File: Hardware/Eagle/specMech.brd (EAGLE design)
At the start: 142.2 x 121.9 mm, 82 parts, among them J1 PINHD-1X8-MOLEX-SHROUD, J2 Molex 0022232081, J3 PINHD-1X8-MOLEX-SHROUD, J4 PINHD-1X8-MOLEX-SHROUD, J5 XPORT, J6 Molex 0022232081, J7 Molex 0022232081, J8 Molex 0022232081, U1 MCP23008-E/SO, U10 ADS1115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

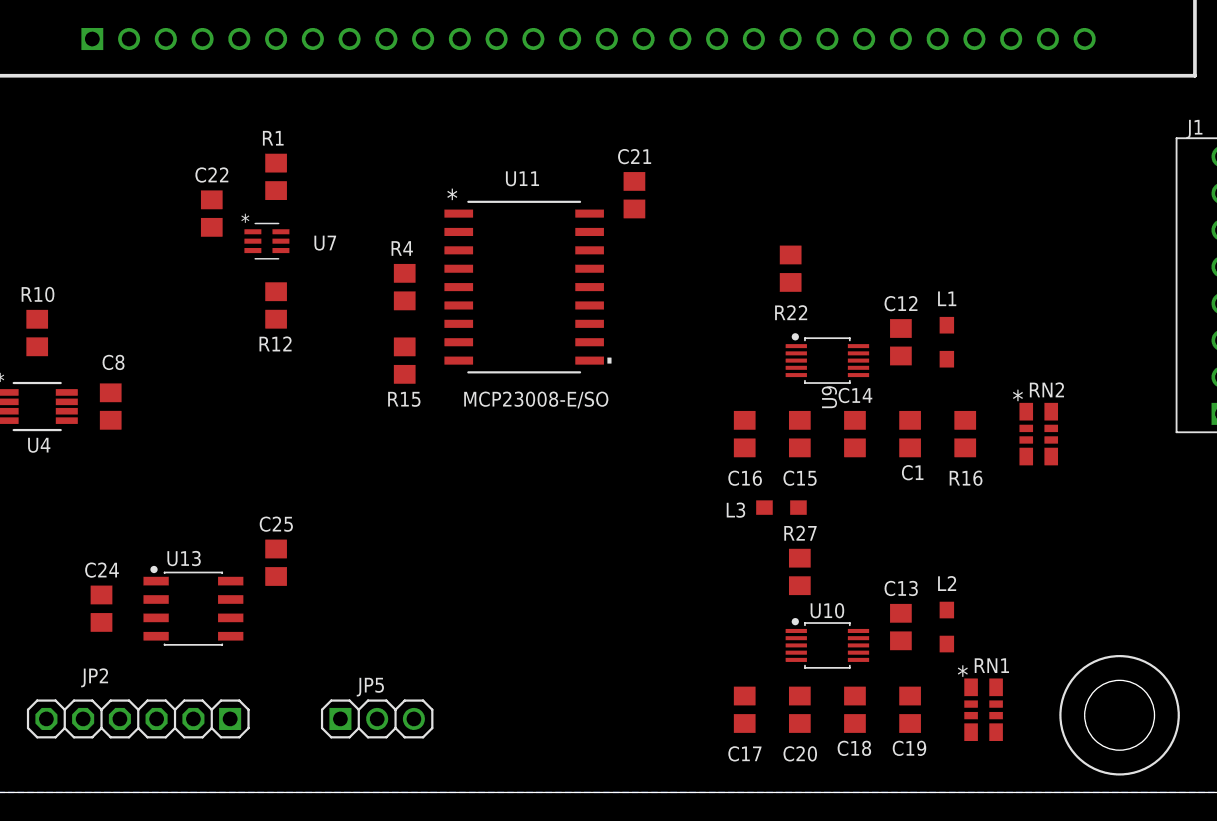
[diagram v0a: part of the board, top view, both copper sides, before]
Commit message: Rearrange ADC chips after brd file recovery
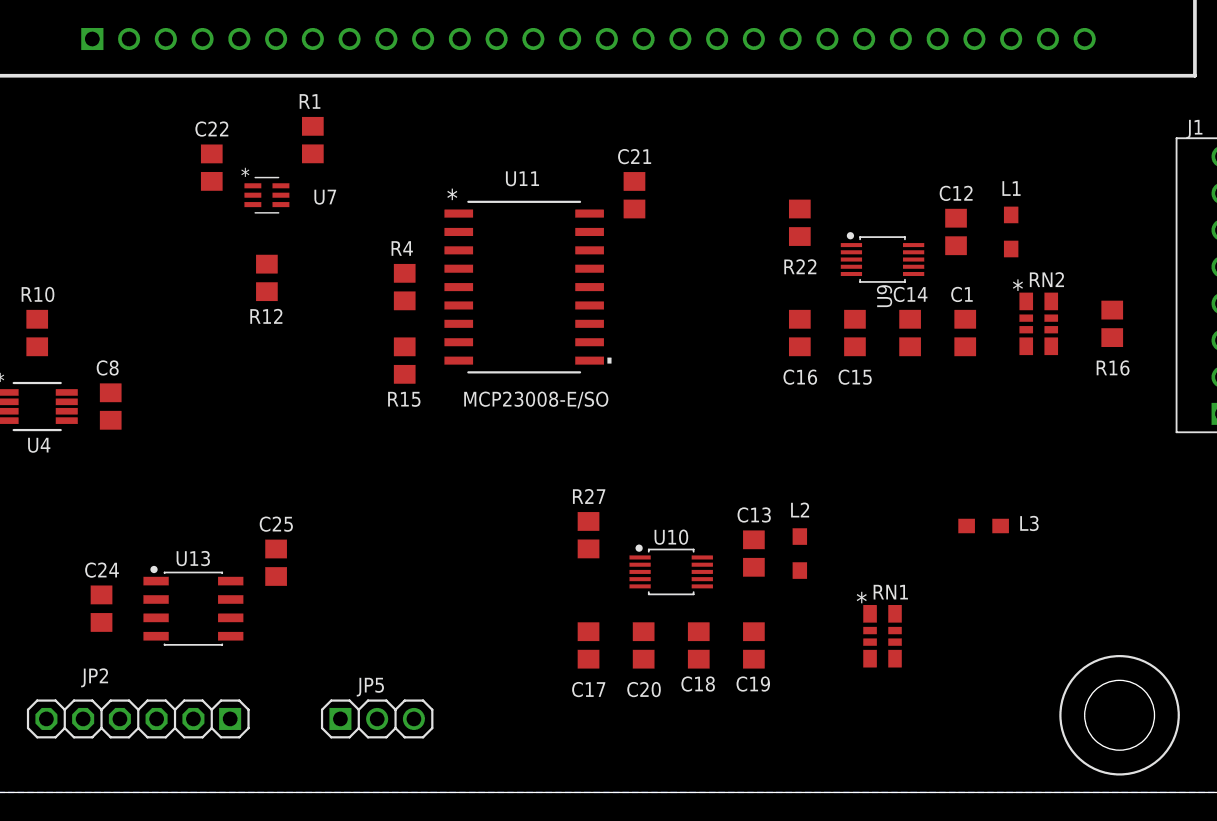
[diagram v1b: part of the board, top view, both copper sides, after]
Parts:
- moved R27 14.8 mm to (85.7, 17.8)
- moved L3 14.0 mm to (113.0, 18.4), turned to 0 degrees
- moved R16 12.7 mm to (121.9, 32.4)
- moved U10 11.9 mm to (91.4, 15.2)
- moved C17 11.7 mm to (85.7, 10.2)
- moved C18 11.7 mm to (93.3, 10.2)
- moved C19 11.7 mm to (97.2, 10.2)
- moved C20 11.7 mm to (89.5, 10.2)
- moved C13 11.4 mm to (97.2, 16.5)
- moved L2 11.4 mm to (100.3, 16.5)
- moved L1 8.82 mm to (114.9, 38.7)
- moved RN1 8.64 mm to (106.0, 10.8)
- moved C12 8.52 mm to (111.1, 38.7)
- moved C1 7.96 mm to (111.8, 31.8), turned to 90 degrees
- moved C14 7.96 mm to (108.0, 31.8)
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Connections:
- removed net 3.3V: C7.1, VR2.VOUT
- net +3.3V: now also C7.1, VR2.VOUT

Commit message: Rearranging parts
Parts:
- removed J2, J7: Molex 0022232081, AUmlib:1X08-MOLEX-SHROUD
- moved C23 19.9 mm to (130.2, 76.2)
- moved U12 19.9 mm to (125.7, 74.9)
- moved C25 3.24 mm to (64.8, 12.7), turned to 270 degrees
- moved C22 1.27 mm to (59.7, 41.9), turned to 270 degrees
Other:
- board text added: "AD590 on/off"
- board text added: "Beeper"
- board text added: "Collimator Motors"
- board text added: "LN2 Controller"
- board text added: "OLED Display"
- board text added: "Pneu Sensors"
- board text added: "Temperature"

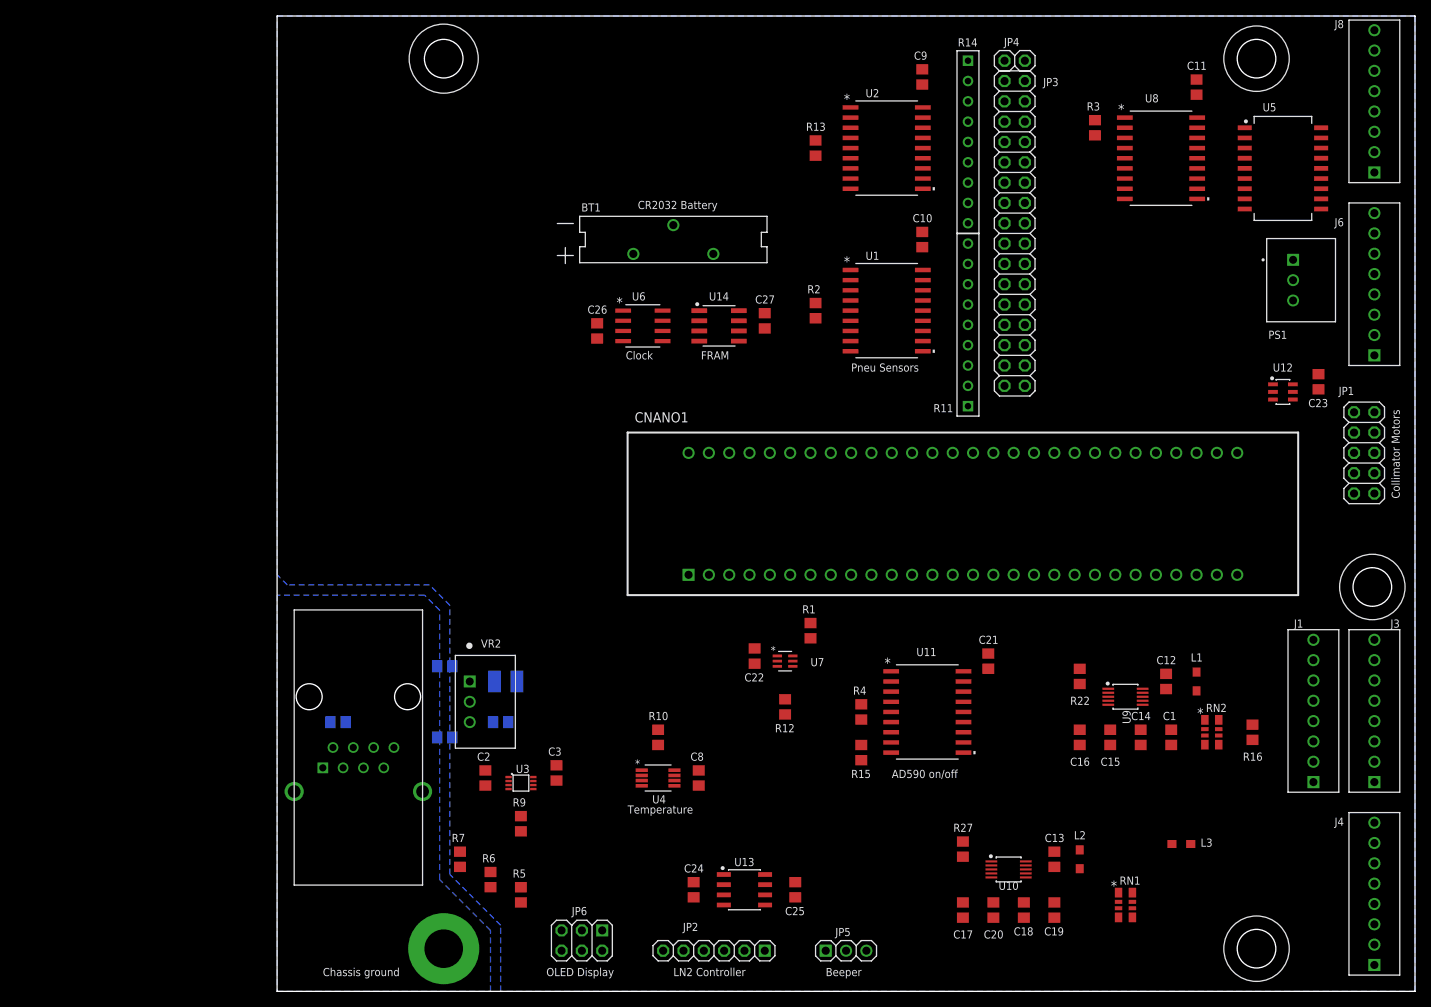
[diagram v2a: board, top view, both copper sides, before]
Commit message: Added ADC ground plane
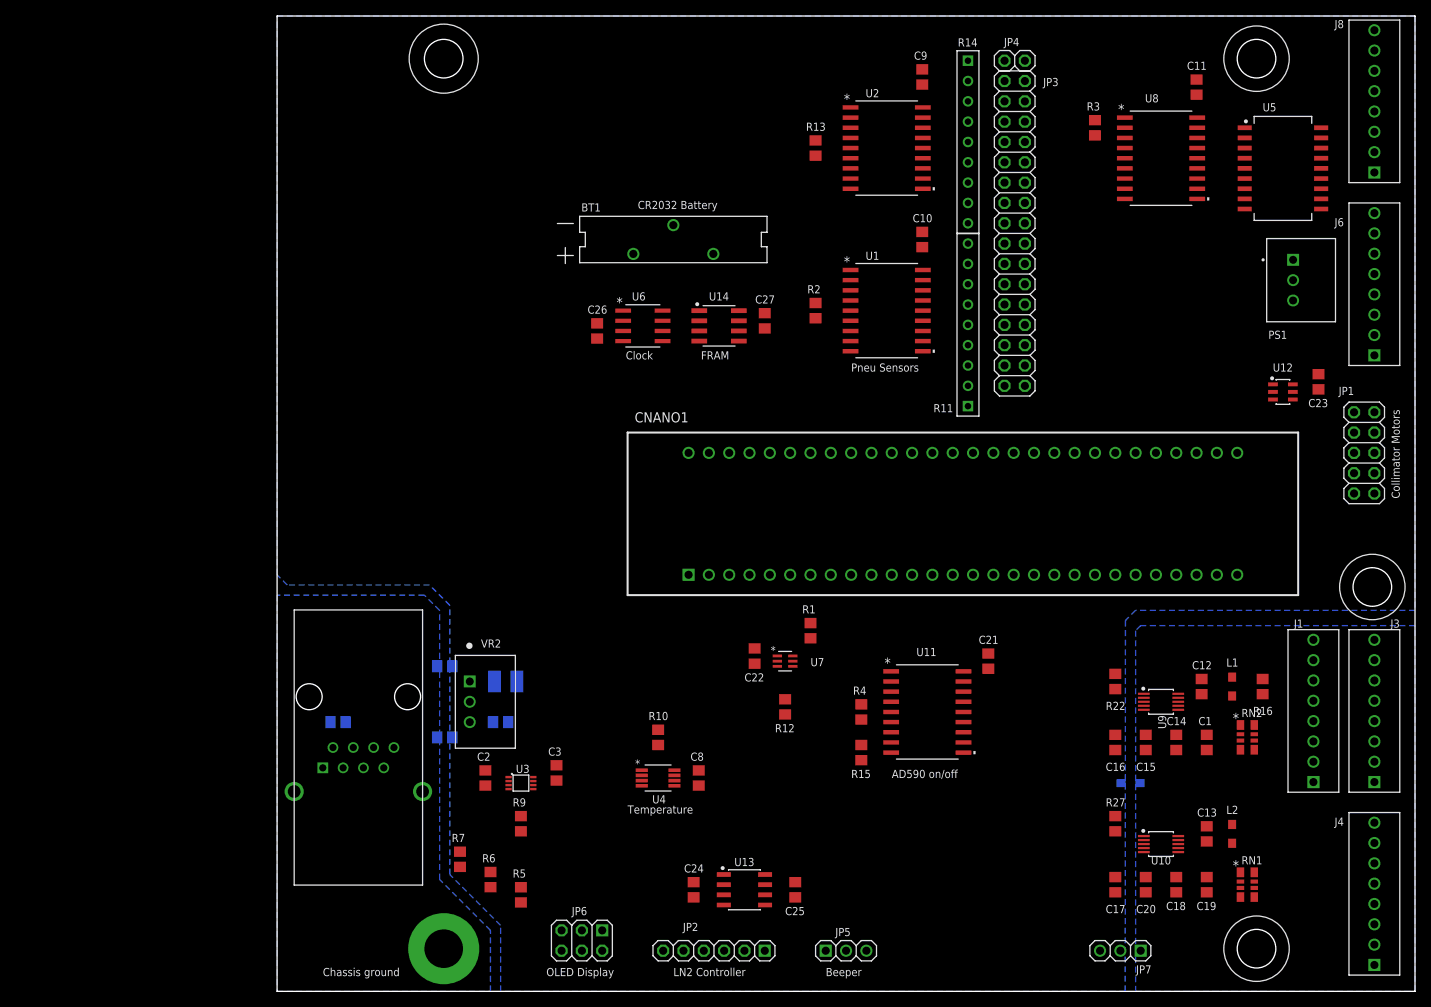
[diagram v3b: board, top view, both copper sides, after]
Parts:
- added JP7: (no value), AUmlib:1X03
- moved C17 19.3 mm to (104.8, 13.3)
- moved R27 19.3 mm to (104.8, 21.0)
- moved C18 19.3 mm to (112.4, 13.3)
- moved C19 19.3 mm to (116.2, 13.3)
- moved C20 19.3 mm to (108.6, 13.3)
- moved C13 19.3 mm to (116.2, 19.7)
- moved L2 19.3 mm to (119.4, 19.7)
- moved U10 19.3 mm to (110.5, 18.4)
- moved RN1 15.5 mm to (121.3, 13.3)
- moved L3 9.92 mm to (106.7, 26.0), flipped to the bottom, turned to 180 degrees
- moved R16 5.85 mm to (123.2, 38.1)
- moved C16 4.49 mm to (104.8, 31.1)
- moved R22 4.49 mm to (104.8, 38.7)
- moved C1 4.49 mm to (116.2, 31.1)
- moved C12 4.49 mm to (115.6, 38.1)
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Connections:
- net GND: now also JP7.2; no longer J1.P$1, J1.P$3, J1.P$5, J1.P$7, J4.P$1, J4.P$3, J4.P$5, J4.P$7
- net GND-ISO: now also J1.P$1, J1.P$3, J1.P$5, J1.P$7, J4.P$1, J4.P$3, J4.P$5, J4.P$7, JP7.1
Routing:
- added copper zone on layer 16, net GND-ISO

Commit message: Routed high current lines
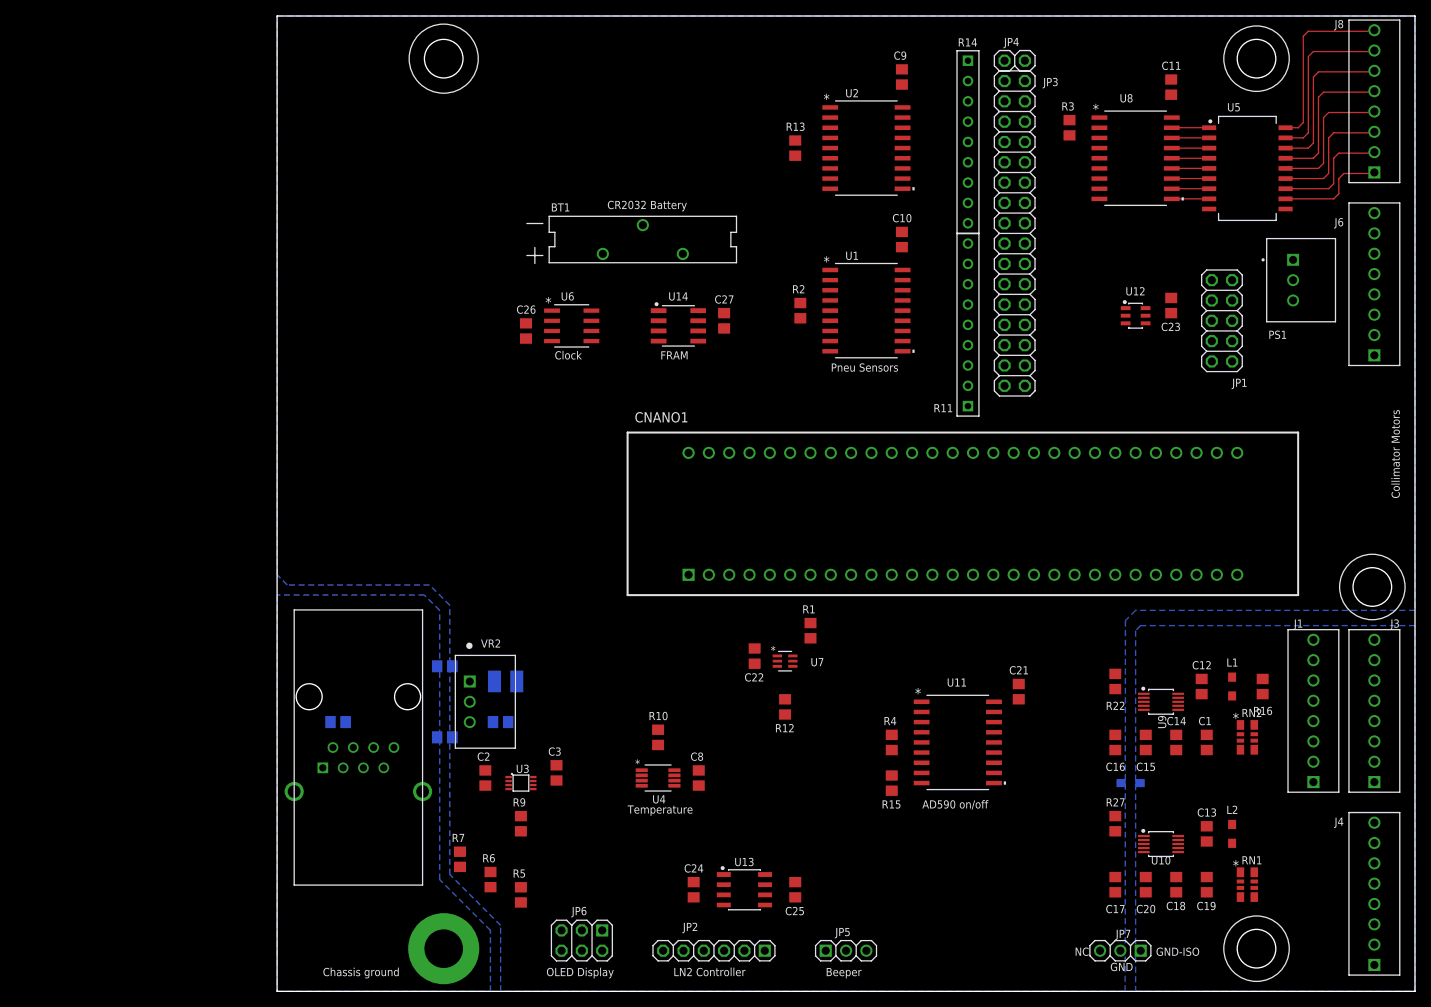
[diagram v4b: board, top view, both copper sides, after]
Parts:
- moved JP1 24.3 mm to (118.1, 83.8), turned to 270 degrees
- moved C23 20.7 mm to (111.8, 85.7)
- moved U12 20.7 mm to (107.3, 84.5)
- moved C26 8.89 mm to (31.1, 82.5)
- moved U6 8.89 mm to (36.8, 83.2)
- moved U11 5.39 mm to (85.1, 31.1)
- moved R15 5.39 mm to (76.8, 26.0)
- moved R4 5.39 mm to (76.8, 31.1)
- moved C21 5.39 mm to (92.7, 37.5)
- moved C27 5.08 mm to (55.9, 83.8)
- moved U14 5.08 mm to (50.2, 83.2)
- moved U5 4.45 mm to (121.3, 102.9)
- moved BT1 3.81 mm to (45.7, 94.0)
- moved C11 3.17 mm to (111.8, 113.0)
- moved R3 3.17 mm to (99.1, 108.0)
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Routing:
- net N$50: track 0.00 -> 22.5 mm
- net N$57: track 0.00 -> 21.2 mm
- net N$56: track 0.00 -> 19.9 mm
- net N$55: track 0.00 -> 18.7 mm
- net N$54: track 0.00 -> 17.4 mm
- net N$53: track 0.00 -> 16.1 mm
- net N$52: track 0.00 -> 14.9 mm
- net N$51: track 0.00 -> 13.6 mm
- net N$48: track 0.00 -> 4.68 mm
- net N$47: track 0.00 -> 4.68 mm
- net N$46: track 0.00 -> 4.68 mm
- net N$45: track 0.00 -> 4.68 mm
- net N$44: track 0.00 -> 4.68 mm
- net N$39: track 0.00 -> 4.68 mm
- net N$38: track 0.00 -> 4.68 mm
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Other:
- board text added: "GND"
- board text added: "GND-ISO"
- board text added: "NC"

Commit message: Wiring
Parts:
- moved C12 2.54 mm to (115.6, 40.6)
- moved L1 2.54 mm to (119.4, 40.6)
- moved R16 2.54 mm to (123.2, 40.6)
- moved R22 2.54 mm to (104.8, 41.3)
- moved U9 2.54 mm to (110.5, 38.7)
- moved C10 1.27 mm to (76.8, 94.0)
- moved C9 1.27 mm to (76.8, 114.3)
- moved R13 1.27 mm to (63.5, 105.4)
- moved R2 1.27 mm to (64.1, 85.1)
- moved U1 1.27 mm to (72.4, 85.1)
- moved U2 1.27 mm to (72.4, 105.4)
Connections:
- net N$19: now also JP1.3; no longer JP1.7
- net N$8: now also JP1.7; no longer JP1.3
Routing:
- net +5V: track 0.00 -> 94.1 mm
- net RC-RX: track 0.00 -> 48.6 mm
- net RC-TX: track 0.00 -> 47.2 mm
- net GND: track 0.00 -> 43.6 mm, vias 0 -> 17
- net +12V: track 0.00 -> 30.4 mm
- net N$16: track 0.00 -> 15.9 mm
- net N$1: track 0.00 -> 15.9 mm
- net N$9: track 0.00 -> 15.9 mm
- net N$22: track 0.00 -> 15.9 mm
- net N$10: track 0.00 -> 15.5 mm
- net N$21: track 0.00 -> 15.4 mm
- net N$2: track 0.00 -> 15.4 mm
- net N$15: track 0.00 -> 15.4 mm
- net N$20: track 0.00 -> 15.0 mm
- net N$11: track 0.00 -> 14.9 mm
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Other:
- board text added: "Collimator Motors USART"
- board text removed: "Collimator Motors"

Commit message: Wiring
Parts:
- moved R12 6.48 mm to (69.8, 36.8)
- moved C22 5.08 mm to (64.8, 41.9)
- moved U7 5.08 mm to (68.6, 41.3)
- moved R1 3.24 mm to (69.8, 45.7)
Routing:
- net SCL: track 0.00 -> 18.8 mm
- net GND: track 43.6 -> 58.6 mm, vias 17 -> 19
- net SDA: track 0.00 -> 11.6 mm
- net +5V: track 94.1 -> 97.2 mm

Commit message: Wiring
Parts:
- moved C18 3.86 mm to (116.2, 12.7)
- moved C19 3.86 mm to (112.4, 12.7)
- moved RN1 0.90 mm to (120.7, 12.7)
- moved C17 0.64 mm to (104.8, 12.7)
- moved C20 0.64 mm to (108.6, 12.7)
- moved L3 0.64 mm to (106.7, 25.4)
- moved C13 0.63 mm to (116.2, 19.1)
- moved L2 0.63 mm to (119.4, 19.1)
- moved R27 0.63 mm to (104.8, 20.3)
- turned C1 to 270 degrees
- turned C14 to 270 degrees
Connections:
- net GND: no longer C12.2, C13.2, U9.1
- net GND-ISO: now also C12.2, C13.2, U9.1
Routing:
- net N$69: track 0.00 -> 32.2 mm
- net A0B: track 0.00 -> 22.4 mm
- net N$68: track 0.00 -> 21.5 mm
- net GND-ISO: track 0.00 -> 19.9 mm, vias 0 -> 5
- net A1B: track 0.00 -> 18.0 mm
- net A3B: track 0.00 -> 17.8 mm
- net A2B: track 0.00 -> 16.2 mm
- net N$65: track 0.00 -> 15.8 mm
- net VBAT1: track 0.00 -> 10.0 mm
- net N$67: track 0.00 -> 9.05 mm
- net N$6: track 0.00 -> 6.96 mm
- net N$70: track 0.00 -> 4.08 mm

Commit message: Wiring
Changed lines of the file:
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@@
 </layers>
 <board>
-<fusionsync huburn="a.cGVyc29uYWw6dWUyZDgyNjcx" projecturn="a.cGVyc29uYWw6dWUyZDgyNjcxIzIwMTgxMjIwMTY2NDc1MjMx" f3durn="urn:adsk.wipprod:dm.lineage:_sV9k5X2SmWQ17yhuORBVg" pcbguid="" lastpulledtime="" lastsyncedchangeguid="" latestrevisionid="a685aebe-6f30-4309-919d-8c6f5bc8299c" lastsyncedrevisionid="a685aebe-6f30-4309-919d-8c6f5bc8299c" lastboardhashguid="185580c9-e881-60b1-63ba-49ad7843264c" lastpushedtime="2020-11-01T21:32:16Z" linktopcb3d="true"/>
+<fusionsync huburn="a.cGVyc29uYWw6dWUyZDgyNjcx" projecturn="a.cGVyc29uYWw6dWUyZDgyNjcxIzIwMTgxMjIwMTY2NDc1MjMx" f3durn="urn:adsk.wipprod:dm.lineage:_sV9k5X2SmWQ17yhuORBVg" pcbguid="" lastpulledtime="" lastsyncedchangeguid="" latestrevisionid="f88995e2-ef19-4b81-bcde-88b136ebe312" lastsyncedrevisionid="f88995e2-ef19-4b81-bcde-88b136ebe312" lastboardhashguid="351dc84e-53f2-6048-b294-c2d578f670e1" lastpushedtime="2020-11-02T02:08:29Z" linktopcb3d="true"/>
 <plain>
 <wire x1="0" y1="0" x2="142.24" y2="0" width="0" layer="20"/>
@@
 <contactref element="R11" pad="7"/>
 <wire x1="86.36" y1="88.392" x2="86.233" y2="88.265" width="0.1524" layer="1"/>
-<wire x1="83.82" y1="88.265" x2="81.915" y2="86.36" width="0.1524" layer="1"/>
-<wire x1="81.915" y1="86.36" x2="76.9112" y2="86.36" width="0.1524" layer="1"/>
-<wire x1="86.233" y1="88.265" x2="83.82" y2="88.265" width="0.1524" layer="1"/>
+<wire x1="84.455" y1="88.265" x2="82.55" y2="86.36" width="0.1524" layer="1"/>
+<wire x1="82.55" y1="86.36" x2="76.9112" y2="86.36" width="0.1524" layer="1"/>
+<wire x1="86.233" y1="88.265" x2="84.455" y2="88.265" width="0.1524" layer="1"/>
 <wire x1="86.36" y1="88.392" x2="90.932" y2="88.392" width="0.1524" layer="1"/>
 </signal>
@@
 <wire x1="112.395" y1="30.165" x2="108.585" y2="30.165" width="0" layer="19" extent="1-1"/>
 <wire x1="116.205" y1="30.165" x2="112.395" y2="30.165" width="0" layer="19" extent="1-1"/>
-<wire x1="108.3404" y1="38.735" x2="112.395" y2="30.165" width="0" layer="19" extent="1-1"/>
-<wire x1="108.3404" y1="39.735" x2="108.3404" y2="38.735" width="0" layer="19" extent="1-1"/>
-<wire x1="115.57" y1="41.59" x2="108.3404" y2="39.735" width="0" layer="19" extent="1-1"/>
+<wire x1="115.57" y1="41.59" x2="123.19" y2="39.69" width="0" layer="19" extent="1-1"/>
+<wire x1="108.3404" y1="39.735" x2="115.57" y2="41.59" width="0" layer="19" extent="1-1"/>
+<wire x1="108.3404" y1="38.735" x2="108.3404" y2="39.735" width="0" layer="19" extent="1-1"/>
 </signal>
 <signal name="N$7">
